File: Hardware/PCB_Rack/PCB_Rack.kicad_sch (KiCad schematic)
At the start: 5 parts, among them J1 Conn_01x03, U1 STM32G431KBTx

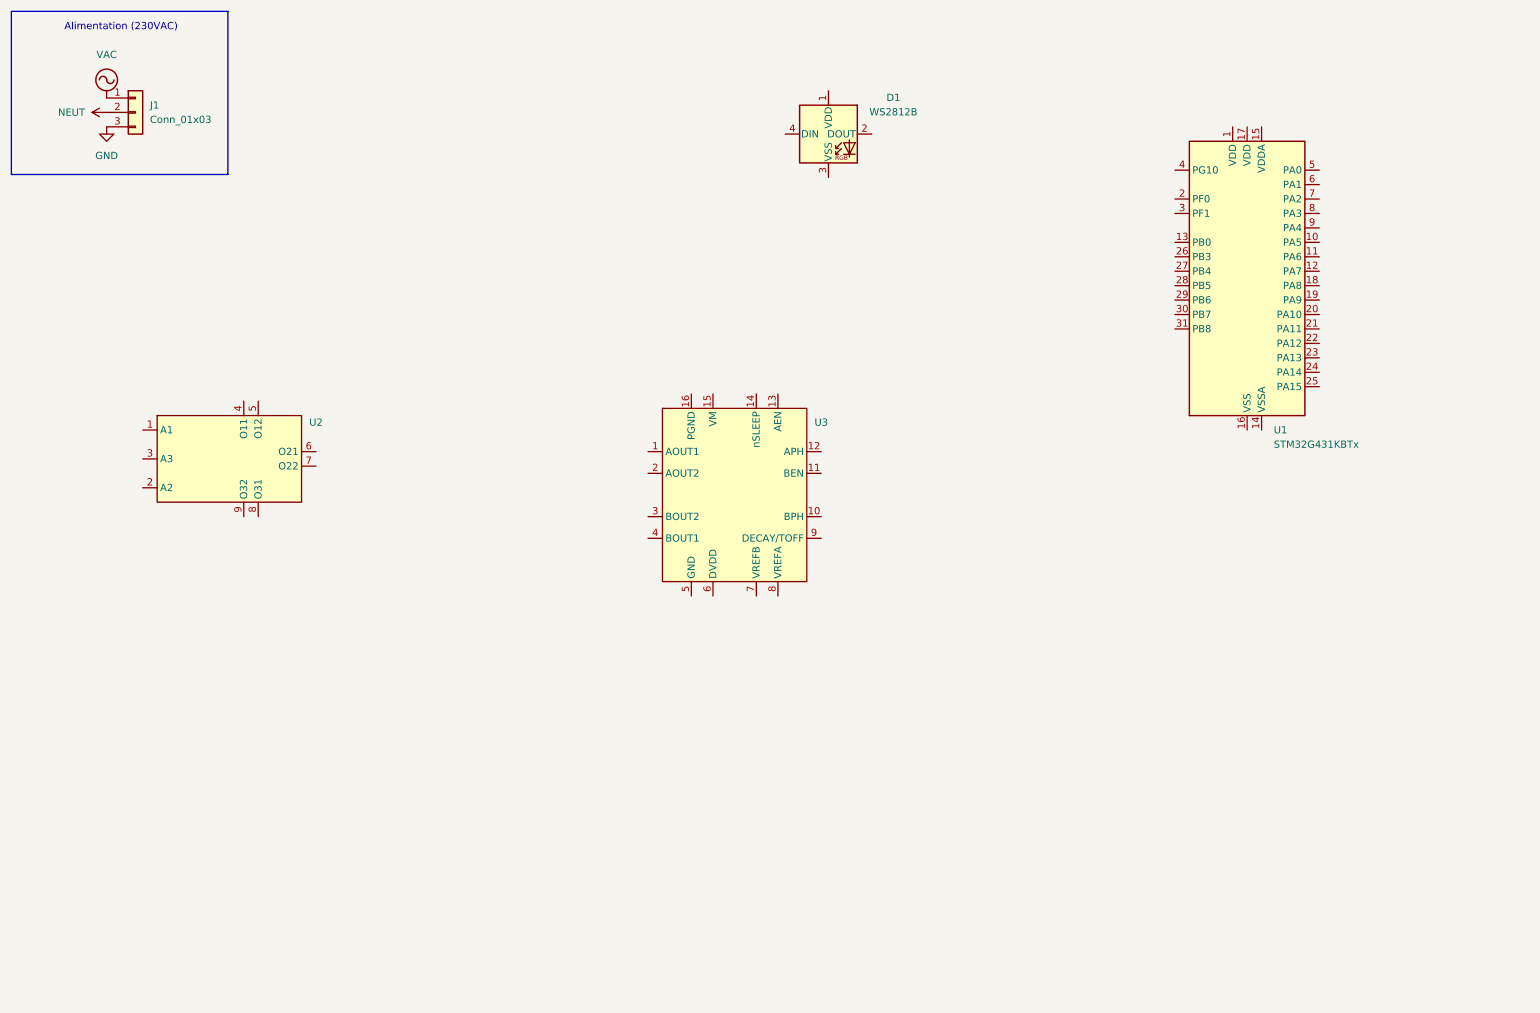
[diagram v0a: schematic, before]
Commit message: finalisation Schematic du PCB Rack
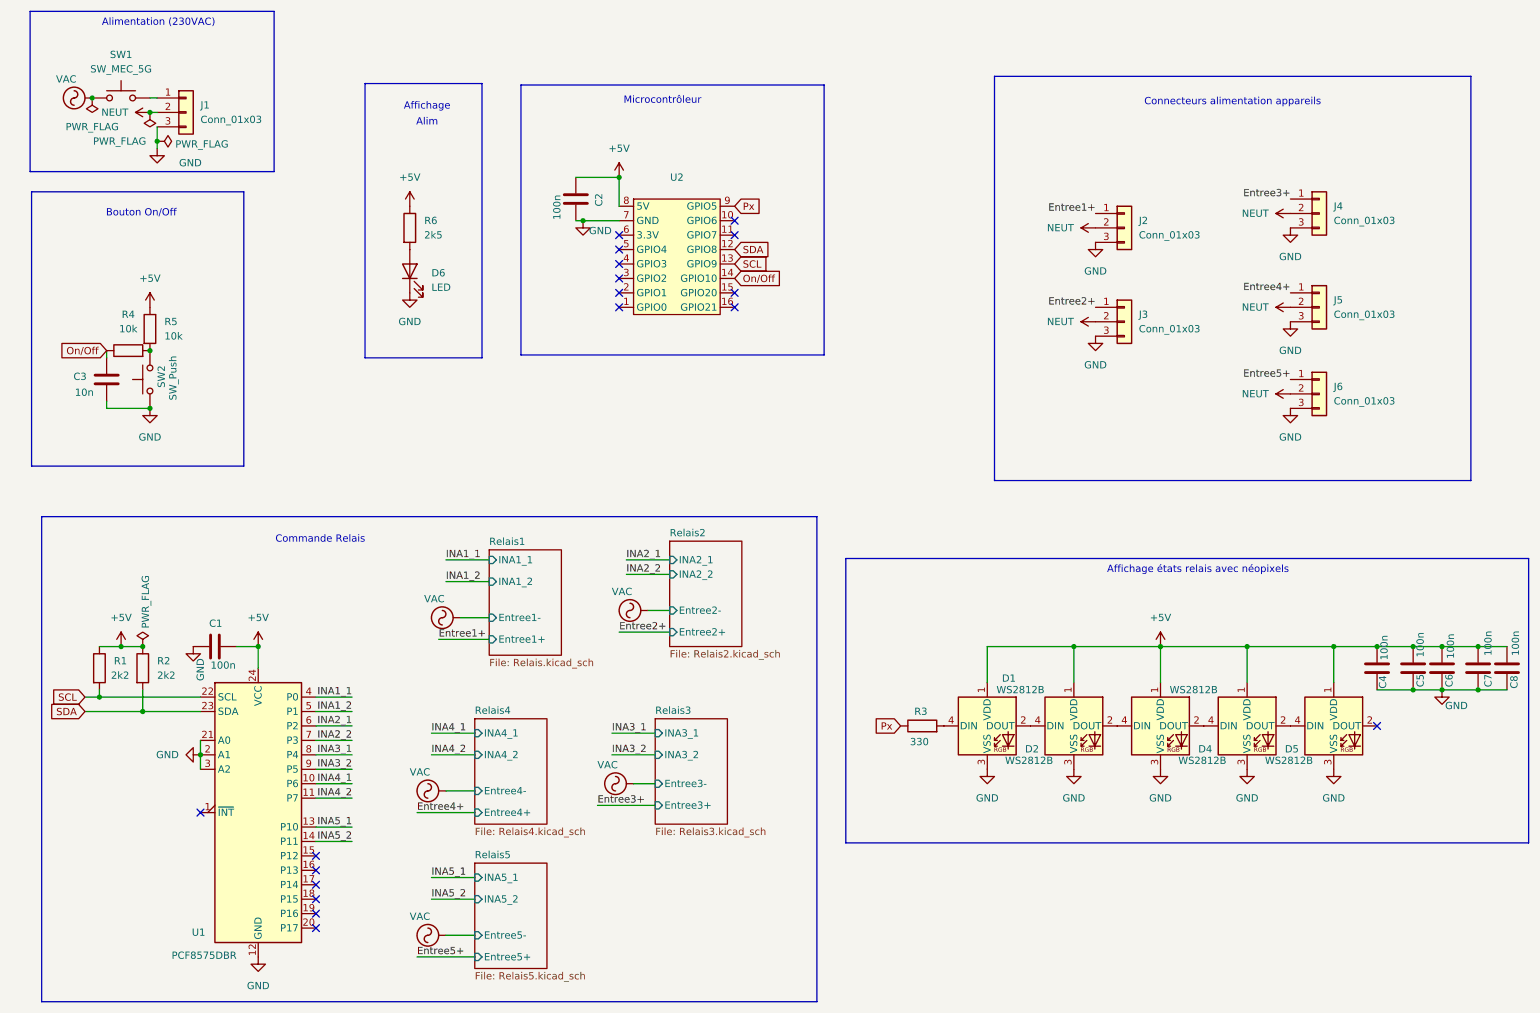
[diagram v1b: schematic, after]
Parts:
- removed U1: STM32G431KBTx, Package_QFP:LQFP-32_7x7mm_P0.8mm, symbol MCU_ST_STM32G4:STM32G431KBTx
- removed U2: ~, symbol RT1_bistable:RT314F05_1
- removed U3: ~, symbol DRV8428E:16-Pin_HTSSOP_1
- added C1, C2, C4, C5, C6, C7, C8: 100n, Capacitor_SMD:C_0603_1608Metric_Pad1.08x0.95mm_HandSolder, symbol Device:C
- added C3: 10n, symbol Device:C
- added D2, D3, D4, D5: WS2812B, LED_SMD:LED_WS2812B_PLCC4_5.0x5.0mm_P3.2mm, symbol LED:WS2812B
- added D6: LED, LED_SMD:LED_0603_1608Metric_Pad1.05x0.95mm_HandSolder, symbol Device:LED
- added J2, J3, J4, J5, J6: Conn_01x03, symbol Connector_Generic:Conn_01x03
- added R1, R2: 2k2, Resistor_SMD:R_0603_1608Metric_Pad0.98x0.95mm_HandSolder, symbol Device:R
- added R3: 330, Resistor_SMD:R_0603_1608Metric_Pad0.98x0.95mm_HandSolder, symbol Device:R
- added R4, R5: 10k, Resistor_SMD:R_0603_1608Metric_Pad0.98x0.95mm_HandSolder, symbol Device:R
- added R6: 2k5, Resistor_SMD:R_0603_1608Metric_Pad0.98x0.95mm_HandSolder, symbol Device:R
- added SW1: SW_MEC_5G, symbol Switch:SW_MEC_5G
- added SW2: SW_Push, symbol Switch:SW_Push
- added U1: PCF8575DBR, Package_SO:SSOP-24_5.3x8.2mm_P0.65mm, symbol Interface_Expansion:PCF8575DBR
- added U2: ~, ESP32_C3_SuperMini:C3_SuperMini, symbol ESP32_C3_SuperMini:SuperMini_1
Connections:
- net GND: now also D1.3 (VSS), C1.1, C2.2, C3.2, C4.2, C5.2, C6.2, C7.2, C8.2, D2.3 (VSS), D3.3 (VSS), D4.3 (VSS), D5.3 (VSS), D6.1 (K), J2.3 (Pin_3), J3.3 (Pin_3), J4.3 (Pin_3), J5.3 (Pin_3), J6.3 (Pin_3), SW2.1, U1.12 (GND), U1.2 (A1), U1.21 (A0), U1.3 (A2), U2.7 (GND)
- net NEUT: now also J2.2 (Pin_2), J3.2 (Pin_2), J4.2 (Pin_2), J5.2 (Pin_2), J6.2 (Pin_2)
- net VAC: now also SW1.1 (A), SW1.2 (A); no longer J1.1 (Pin_1)
- net +5V: now reaches D1.1 (VDD)
- net +5V: now also C1.2, C2.1, C4.1, C5.1, C6.1, C7.1, C8.1, D2.1 (VDD), D3.1 (VDD), D4.1 (VDD), D5.1 (VDD), R1.1, R2.1, R5.1, R6.1, U1.24 (VCC), U2.8 (5V)
- net at D1.2 (DOUT): now also D2.4 (DIN)
- net at D1.4 (DIN): now also R3.2
- new net: R4.2, R5.2, SW2.2
- new net: J1.1 (Pin_1), SW1.3 (B), SW1.4 (B)
- new net: D4.2 (DOUT), D5.4 (DIN)
- new net: D3.2 (DOUT), D4.4 (DIN)
- new net: D2.2 (DOUT), D3.4 (DIN)
- new net: D6.2 (A), R6.2
- new net Entree1+: J2.1 (Pin_1)
- new net Entree2+: J3.1 (Pin_1)
- new net Entree3+: J4.1 (Pin_1)
- new net Entree4+: J5.1 (Pin_1)
- new net Entree5+: J6.1 (Pin_1)
- new net INA1_1: U1.4 (P0)
- new net INA1_2: U1.5 (P1)
- new net INA2_1: U1.6 (P2)
- new net INA2_2: U1.7 (P3)
- new net INA3_1: U1.8 (P4)
- new net INA3_2: U1.9 (P5)
- new net INA4_1: U1.10 (P6)
- new net INA4_2: U1.11 (P7)
- new net INA5_1: U1.13 (P10)
- new net INA5_2: U1.14 (P11)
- new net On/Off: C3.1, R4.1, U2.14 (GPIO10)
- new net Px: R3.1, U2.9 (GPIO5)
- new net SCL: R1.2, U1.22 (SCL), U2.13 (GPIO9)
- new net SDA: R2.2, U1.23 (SDA), U2.12 (GPIO8)
- no-connect marks 0 -> 18
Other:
- added sheet Relais1 (Relais.kicad_sch)
- added sheet Relais2 (Relais2.kicad_sch)
- added sheet Relais3 (Relais3.kicad_sch)
- added sheet Relais4 (Relais4.kicad_sch)
- added sheet Relais5 (Relais5.kicad_sch)
- note added: "Affichage"
- note added: "Affichage états relais avec néopixels"
- note added: "Alim"
- note added: "Bouton On/Off"
- note added: "Commande Relais"
- note added: "Connecteurs alimentation appareils"
- note added: "Microcontrôleur"
- moved on the sheet: D1, J1

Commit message: modification README de la partie HARDWARE, ajout README dans le répertoir PCB Rack
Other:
- title: (none) -> PCB Rack 
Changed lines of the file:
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@@
 	(paper "A4")
 	(title_block
+		(title "PCB Rack ")
 		(date "2025-06-02")
-		(comment 1 "Voici le PCB que je développe durant ce stage")
+		(comment 1 "Capodagli Janus")
+		(comment 2 "Version 1")
 	)
 	(rectangle

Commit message: commit avant pull
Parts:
- R6: value 2k5 -> 2k2
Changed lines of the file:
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@@
 			)
 		)
-		(property "Value" "2k5"
+		(property "Value" "2k2"
 			(at 87.63 53.3399 0)
 			(effects
